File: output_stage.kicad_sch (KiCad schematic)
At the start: 41 parts, among them U2 OPA1612-Q1, U3 OPA1612-Q1, U4 OPA1622

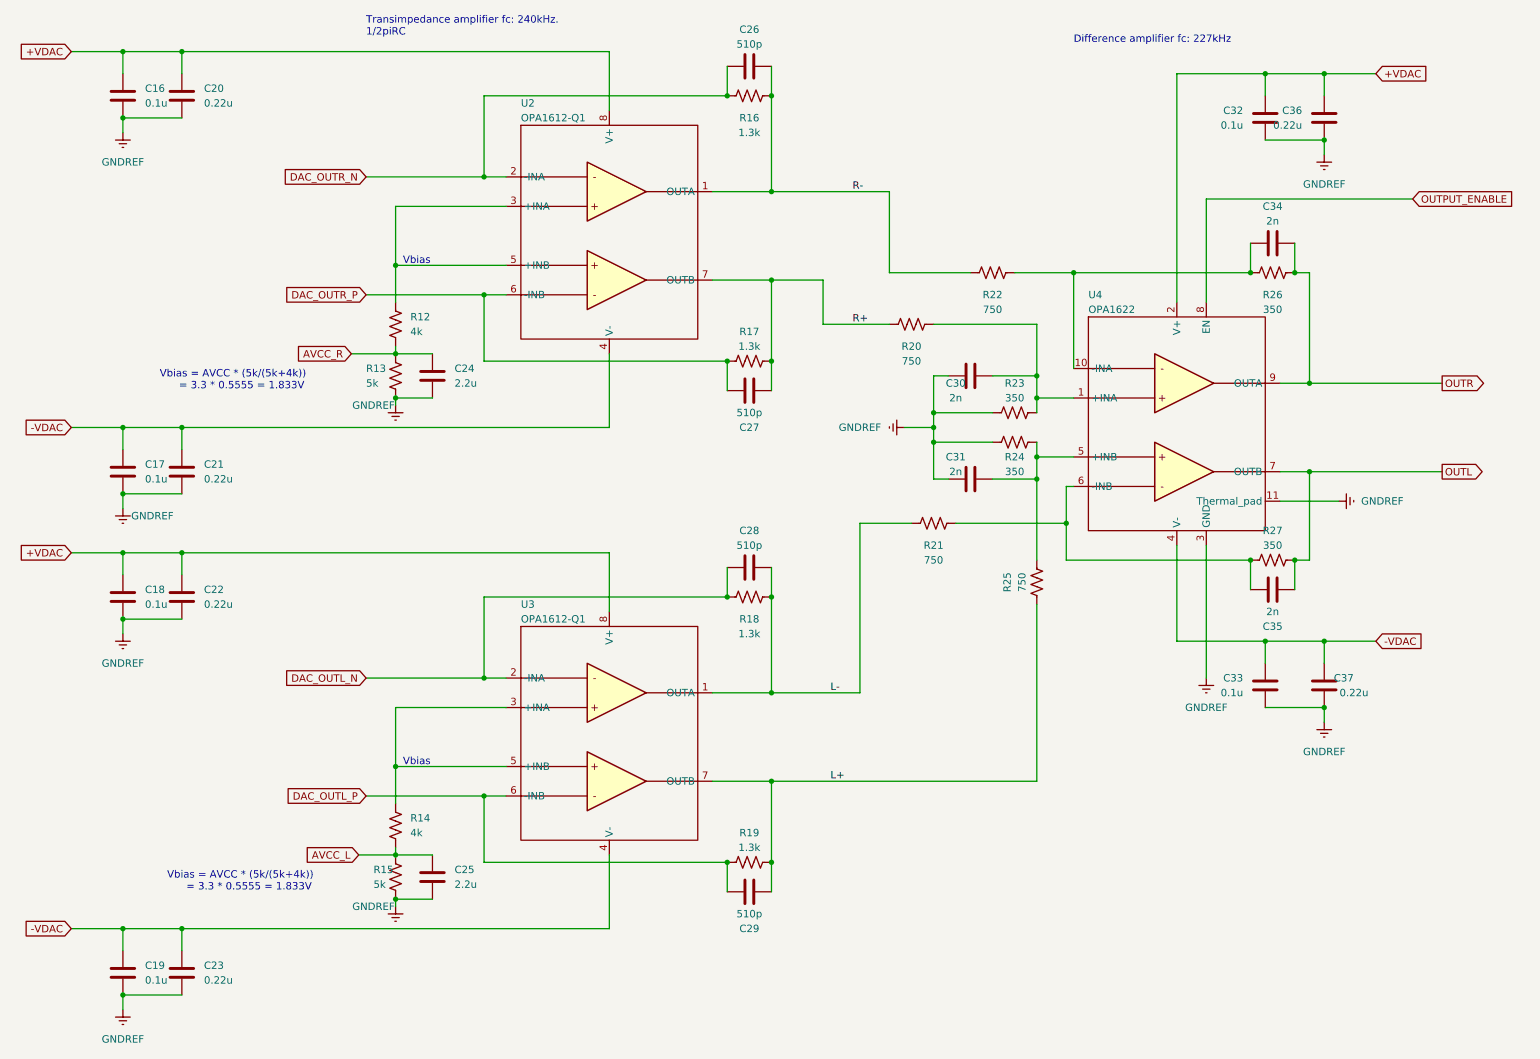
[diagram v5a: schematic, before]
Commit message: Adding footprints. WIP PCB, finished routing, no ground planes yet
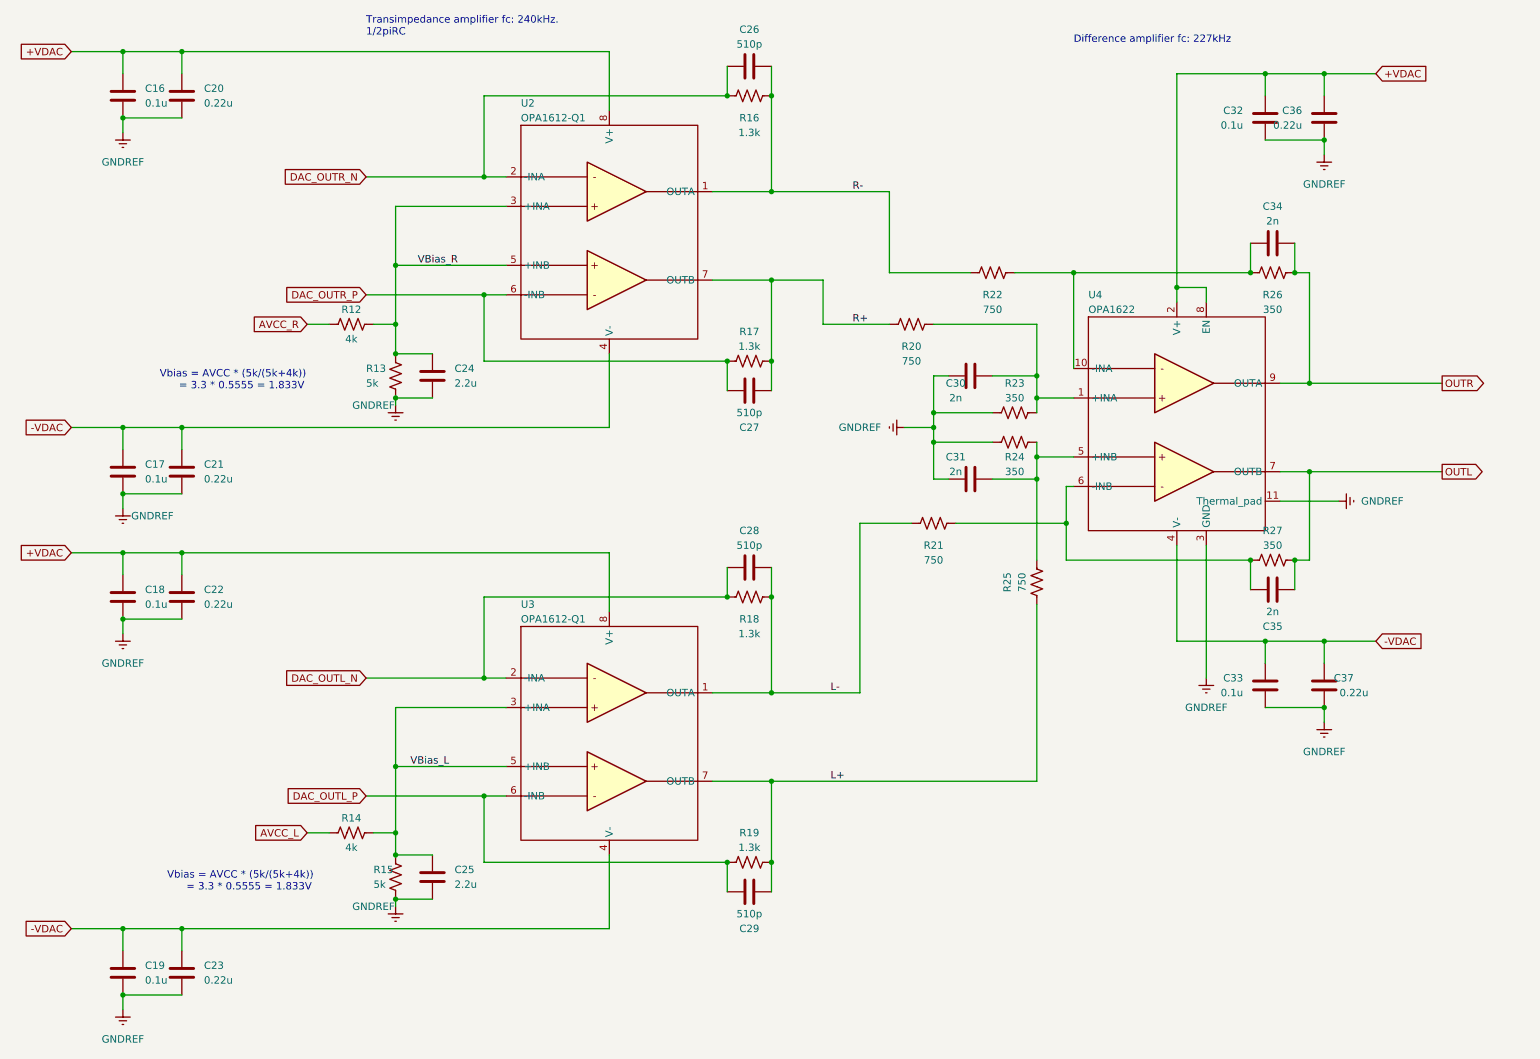
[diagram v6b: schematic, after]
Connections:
- net OUTPUT_ENABLE is gone; now on net +VDAC: U4.8 (EN)
- net AVCC_L: now also R14.2; no longer C25.2, R14.1, R15.2
- net AVCC_R: now also R12.2; no longer C24.2, R12.1, R13.2
- net VBias_L: now reaches U3.3 (+INA), U3.5 (+INB)
- net VBias_L: now also C25.2, R14.1, R15.2; no longer R14.2
- net VBias_R: now reaches U2.3 (+INA), U2.5 (+INB)
- net VBias_R: now also C24.2, R12.1, R13.2; no longer R12.2
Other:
- note removed: "Vbias"
- moved on the sheet: R12, R14

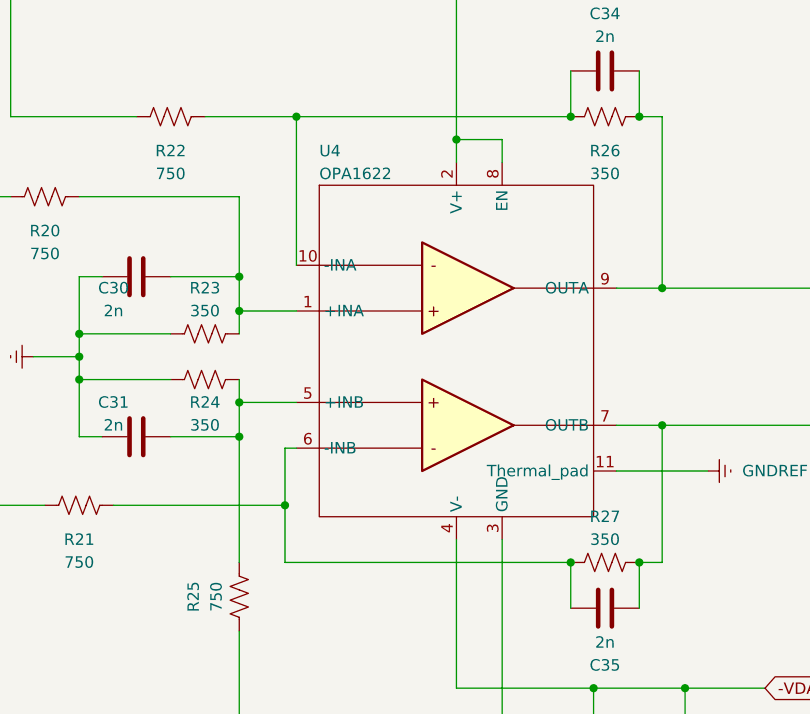
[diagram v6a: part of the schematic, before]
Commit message: Adding part numbers for passives
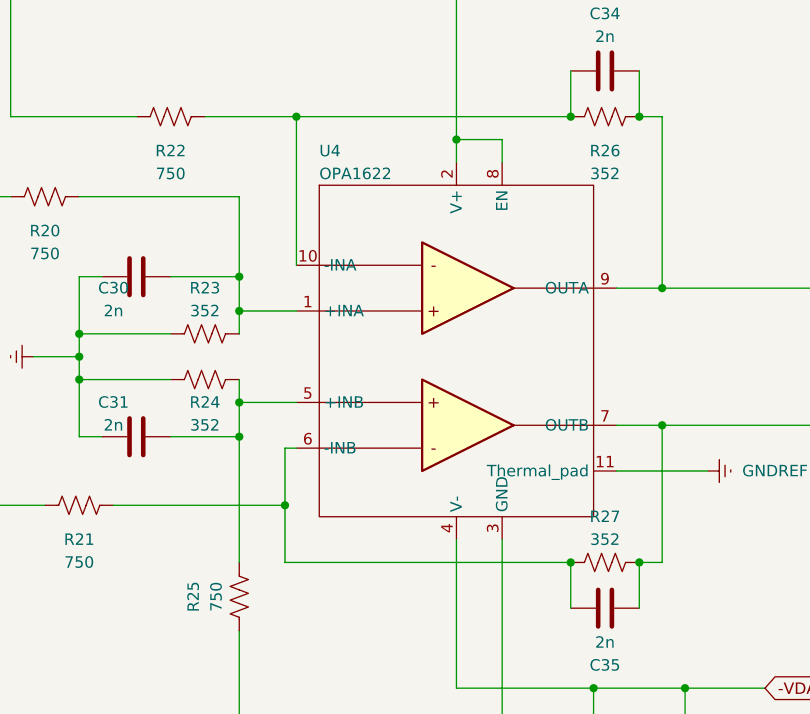
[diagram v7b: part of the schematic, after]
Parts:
- C16, C17, C18, C19: Mouser Part Number (none) -> 187-CL21B104KBCNFNC; Part Number (none) -> CL21B104KBCNFNC
- C20, C21, C22, C23, C36, C37: Mouser Part Number (none) -> 581-0805YC224JAT2A; Part Number (none) -> 0805YC224JAT2A
- C24, C25: Mouser Part Number (none) -> 581-0805ZD225KAT4A; Part Number (none) -> 0805ZD225KAT4A
- C26, C27, C28, C29: Mouser Part Number (none) -> 80-C0805C511F3HACTU; Part Number (none) -> C0805C511F3HACTU
- C30, C31, C34, C35: Mouser Part Number (none) -> 80-C0805C202F4HAUTO; Part Number (none) -> C0805C202F4HACAUTO
- R12, R14: Mouser Part Number (none) -> 71-TNPW08054K02BYEN; Part Number (none) -> TNPW08054K02BYEN
- R13, R15: Mouser Part Number (none) -> 71-PNM0805E5001BST5; Part Number (none) -> PNM0805E5001BST5
- R16, R17, R18, R19: Mouser Part Number (none) -> 754-RG2012P-132-BT5; Part Number (none) -> RG2012P-132-B-T5
- R20, R21, R22, R25: Mouser Part Number (none) -> 71-TNPW0805750RBEEA; Part Number (none) -> TNPW0805750RBEEA
- R23, R24, R26, R27: value 350 -> 352; Mouser Part Number (none) -> 660-RN73H2ATD3520B25; Part Number (none) -> RN73H2ATTD3520B25
- U2, U3: Mouser Part Number (none) -> 595-OPA1612AQDRQ1; Part Number (none) -> OPA1612AQDRQ1
- U4: Arrow Part Number (none) -> OPA1622IDRCR; Arrow Price/Stock (none) -> https://www.arrow.com/en/products/opa1622idrcr/texas-instru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; Manufacturer_Name (none) -> Texas Instruments; Manufacturer_Part_Number (none) -> OPA1622IDRCR; Mouser Part Number (none) -> 595-OPA1622IDRCR; Mouser Price/Stock (none) -> https://www.mouser.co.uk/ProductDetail/Texas-Instruments/OP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

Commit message: Adding more part numbers. WIP verifying part numbers
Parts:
- C32, C33: Mouser Part Number (none) -> 187-CL21B104KBCNFNC; Part Number (none) -> CL21B104KBCNFNC
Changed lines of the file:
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@@
+      (effects (font (size 1.27 1.27)) hide)
+    )
+    (property "Mouser Part Number" "187-CL21B104KBCNFNC" (id 4) (at 232.41 30.48 0)
+      (effects (font (size 1.27 1.27)) hide)
+    )
+    (property "Part Number" "CL21B104KBCNFNC" (id 5) (at 232.41 30.48 0)
       (effects (font (size 1.27 1.27)) hide)
     )
@@
       (effects (font (size 1.27 1.27)) hide)
     )
+    (property "Mouser Part Number" "187-CL21B104KBCNFNC" (id 4) (at 232.41 128.27 0)
+      (effects (font (size 1.27 1.27)) hide)
+    )
+    (property "Part Number" "CL21B104KBCNFNC" (id 5) (at 232.41 128.27 0)
+      (effects (font (size 1.27 1.27)) hide)
+    )
